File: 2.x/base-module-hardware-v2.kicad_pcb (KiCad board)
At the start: 4 copper layers, 99.7 x 99.7 mm, 276 parts, among them K1 CONN_3, P1 PINBALL-CONNECTOR, P2 PINBALL-CONNECTOR, P3 SOLENOID-CONNECTOR, P4 CONN_16, P5 CONN_16, P6 HE10-34, Q1 BC846, Q10 DMN6040SSD, Q11 BC846, Q12 BC846, Q13 DMP2240UDM, Q14 DMP2240UDM, Q15 BC846, Q16 BC846, Q17 BC846, Q18 BC846, Q19 DMN6040SSD, Q2 BC846, Q20 DMN6040SSD, Q21 BC846, Q22 BC846, Q23 BC846, Q24 BC846, Q25 BC846, Q26 BC846, Q27 BC846, Q28 BC846, Q29 BSS138 DNP, Q3 DMN6040SSD, Q30 FDD5614P, Q31 BC846, Q32 BSS138, Q4 DMN6040SSD, Q5 BC846, Q6 BC846, Q7 BC846, Q8 BC846, Q9 DMN6040SSD, U1 74LVC14, U2 STM32F072R, U3 MCP2562, U4 MC78L05, U5 AP1117IE33G, U6 ZXCT1086E5TA, U7 ZXCT1107SA-7, U8 LM7805CT, U9 MMA8653FC, X1 8.000 MHz

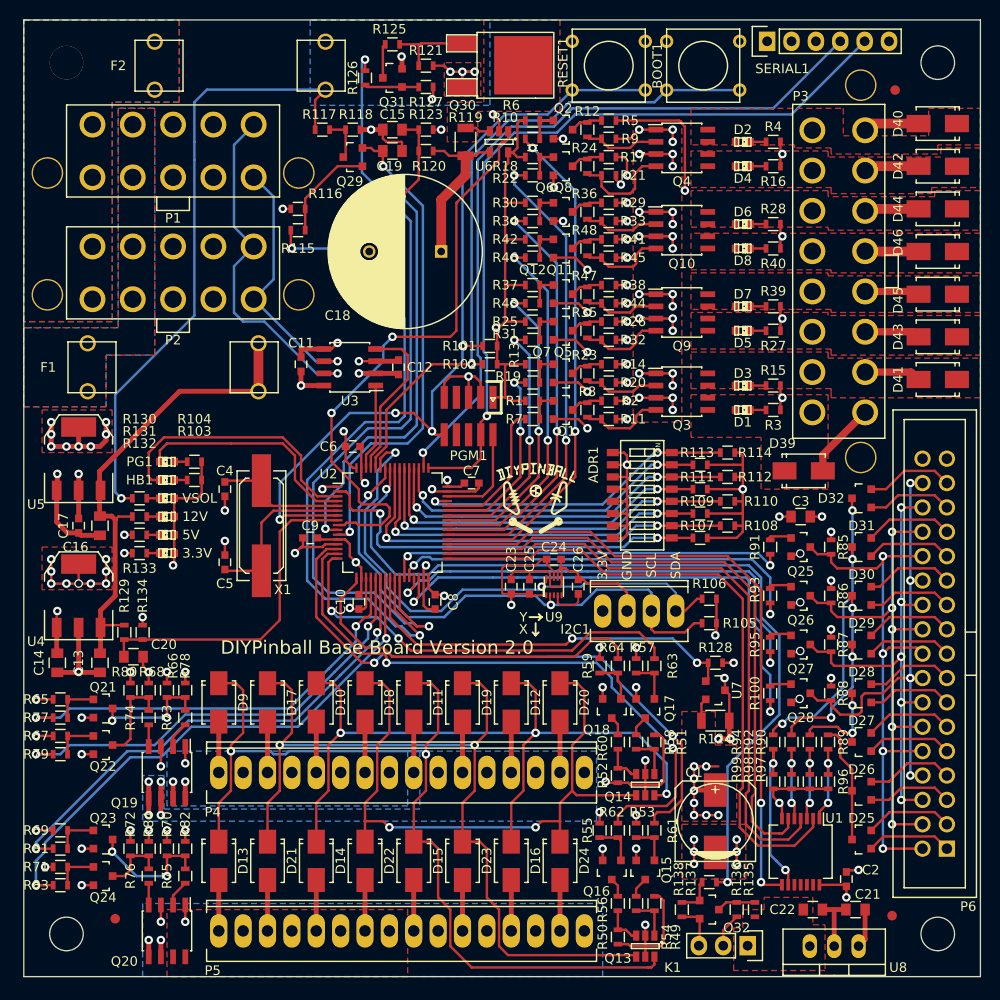
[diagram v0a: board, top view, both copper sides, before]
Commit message: Committing latest files. This includes the KiCAD 4.0.0rc1 migration as well as the updates to Base Board 2.1.
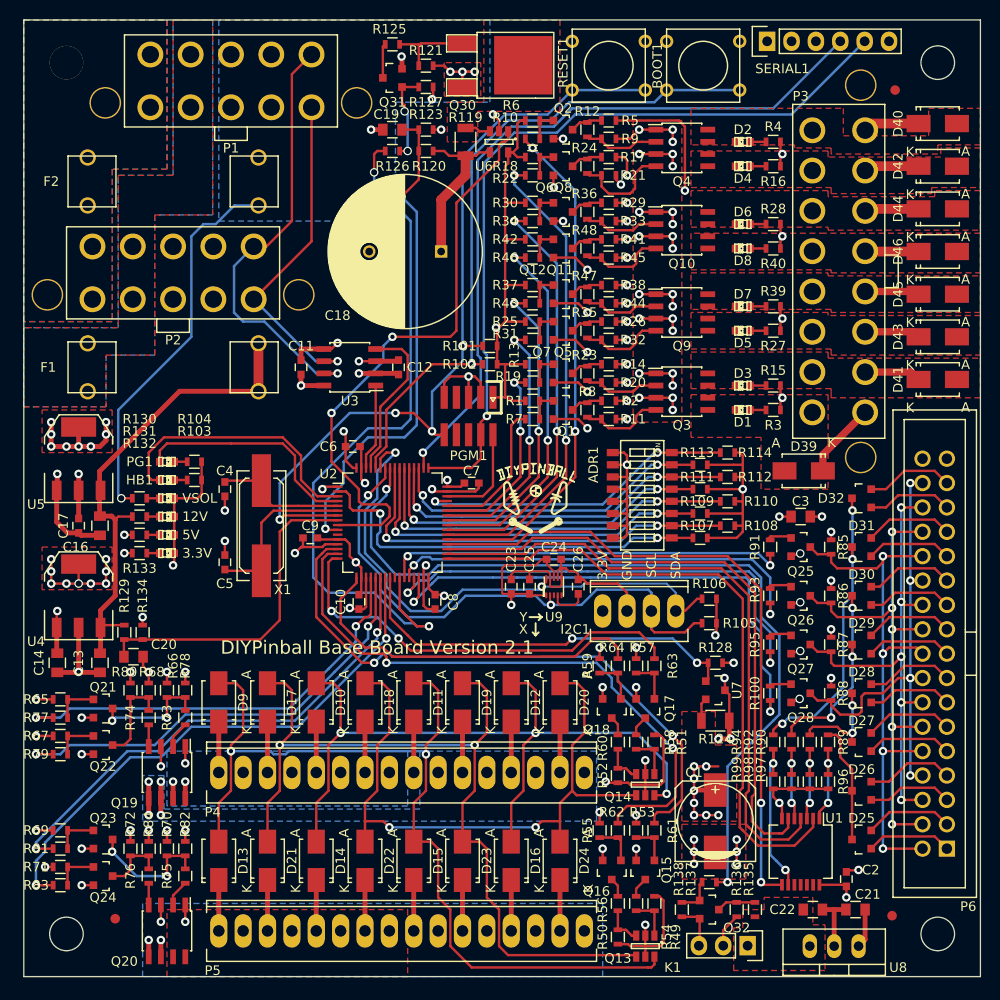
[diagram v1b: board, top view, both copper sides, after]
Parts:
- removed C15: 10u DNP, Capacitors_SMD:C_0805
- removed Q29: BSS138 DNP, Housings_SOT-23_SOT-143_TSOT-6:SOT-23
- removed R115: 1K DNP, Resistors_SMD:R_0603
- removed R116: 10K DNP, Resistors_SMD:R_0603
- removed R117: 95.3K 1% DNP, Resistors_SMD:R_0603
- removed R118: 5.1K 1% DNP, Resistors_SMD:R_0603
- D10, D11, D12, D13, D14, D15, D16, D17, D18, D19, D20, D21, D22, D23, D24, D39, D40, D41, D42, D43, D44, D45, D46, D9: footprint Diodes_SMD:Diode-SMA_Standard -> Diodes_SMD:SMA_Standard
- moved F2 13.9 mm to (71.4, 96.8)
- moved P1 9.47 mm to (77.5, 86.4)
- moved R126 8.14 mm to (94.3, 93.7), turned to 180 degrees
- moved C11 0.32 mm to (84.8, 116.2)
- turned D1 to 0 degrees
- turned D10 to 90 degrees
- turned D11 to 90 degrees
- turned D12 to 90 degrees
- turned D13 to 90 degrees
- turned D14 to 90 degrees
- turned D15 to 90 degrees
- turned D16 to 90 degrees
- turned D17 to 90 degrees
- turned D18 to 90 degrees
- turned D19 to 90 degrees
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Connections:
- net VCC renamed +3.3V
- D12 pad 1: Net-(D10-Pad1) -> Net-(D12-Pad1)
- D12 pad 2: Net-(D12-Pad2) -> Net-(D10-Pad2)
- D13 pad 1: Net-(D11-Pad1) -> Net-(D13-Pad1)
- D13 pad 2: Net-(D13-Pad2) -> Net-(D11-Pad2)
- D14 pad 1: Net-(D10-Pad1) -> Net-(D14-Pad1)
- D14 pad 2: Net-(D14-Pad2) -> Net-(D10-Pad2)
- D15 pad 1: Net-(D11-Pad1) -> Net-(D15-Pad1)
- D15 pad 2: Net-(D15-Pad2) -> Net-(D11-Pad2)
- D16 pad 1: Net-(D10-Pad1) -> Net-(D16-Pad1)
- D16 pad 2: Net-(D16-Pad2) -> Net-(D10-Pad2)
- D19 pad 1: Net-(D17-Pad1) -> Net-(D19-Pad1)
- D19 pad 2: Net-(D19-Pad2) -> Net-(D17-Pad2)
- D20 pad 1: Net-(D18-Pad1) -> Net-(D20-Pad1)
- D20 pad 2: Net-(D20-Pad2) -> Net-(D18-Pad2)
- D21 pad 1: Net-(D17-Pad1) -> Net-(D21-Pad1)
- D21 pad 2: Net-(D21-Pad2) -> Net-(D17-Pad2)
- D22 pad 1: Net-(D18-Pad1) -> Net-(D22-Pad1)
- D22 pad 2: Net-(D22-Pad2) -> Net-(D18-Pad2)
- D23 pad 1: Net-(D17-Pad1) -> Net-(D23-Pad1)
- D23 pad 2: Net-(D23-Pad2) -> Net-(D17-Pad2)
- D24 pad 1: Net-(D18-Pad1) -> Net-(D24-Pad1)
- D24 pad 2: Net-(D24-Pad2) -> Net-(D18-Pad2)
- D35 pad 1: Net-(D35-Pad1) -> GND
- D35 pad 2: GND -> Net-(D35-Pad2)
- D36 pad 1: Net-(D36-Pad1) -> GND
- D36 pad 2: GND -> Net-(D36-Pad2)
- D37 pad 1: Net-(D37-Pad1) -> GND
- D37 pad 2: GND -> Net-(D37-Pad2)
- D38 pad 1: Net-(D38-Pad1) -> GND
- D38 pad 2: GND -> Net-(D38-Pad2)
- D39 pad 1: Net-(D1-Pad2) -> /Solenoid Driver/SOL_PWR
- D39 pad 2: /Solenoid Driver/SOL_PWR -> Net-(D1-Pad1)
- D40 pad 1: Net-(D2-Pad2) -> /Solenoid Driver/SOL_PWR
- D40 pad 2: /Solenoid Driver/SOL_PWR -> Net-(D2-Pad1)
- D41 pad 1: Net-(D3-Pad2) -> /Solenoid Driver/SOL_PWR
- D41 pad 2: /Solenoid Driver/SOL_PWR -> Net-(D3-Pad1)
- D42 pad 1: Net-(D4-Pad2) -> /Solenoid Driver/SOL_PWR
- D42 pad 2: /Solenoid Driver/SOL_PWR -> Net-(D4-Pad1)
- D43 pad 1: Net-(D43-Pad1) -> /Solenoid Driver/SOL_PWR
- D43 pad 2: /Solenoid Driver/SOL_PWR -> Net-(D43-Pad2)
- D44 pad 1: Net-(D44-Pad1) -> /Solenoid Driver/SOL_PWR
- D44 pad 2: /Solenoid Driver/SOL_PWR -> Net-(D44-Pad2)
- D45 pad 1: Net-(D45-Pad1) -> /Solenoid Driver/SOL_PWR
- D45 pad 2: /Solenoid Driver/SOL_PWR -> Net-(D45-Pad2)
- D46 pad 1: Net-(D46-Pad1) -> /Solenoid Driver/SOL_PWR
- D46 pad 2: /Solenoid Driver/SOL_PWR -> Net-(D46-Pad2)
- D5 pad 1: Net-(D5-Pad1) -> Net-(D43-Pad2)
- D5 pad 2: Net-(D43-Pad1) -> Net-(D5-Pad2)
- D6 pad 1: Net-(D6-Pad1) -> Net-(D44-Pad2)
- D6 pad 2: Net-(D44-Pad1) -> Net-(D6-Pad2)
- D7 pad 1: Net-(D7-Pad1) -> Net-(D45-Pad2)
- D7 pad 2: Net-(D45-Pad1) -> Net-(D7-Pad2)
- D8 pad 1: Net-(D8-Pad1) -> Net-(D46-Pad2)
- D8 pad 2: Net-(D46-Pad1) -> Net-(D8-Pad2)
- D9 pad 1: Net-(D11-Pad1) -> Net-(D9-Pad1)
- D9 pad 2: Net-(D9-Pad2) -> Net-(D11-Pad2)
- HB1 pad 1: /Control Logic/HEARTBEAT -> Net-(HB1-Pad1)
- HB1 pad 2: Net-(HB1-Pad2) -> /Control Logic/HEARTBEAT
- P3 pad 1: Net-(D1-Pad2) -> Net-(D1-Pad1)
- P3 pad 2: Net-(D3-Pad2) -> Net-(D3-Pad1)
- P3 pad 3: Net-(D43-Pad1) -> Net-(D43-Pad2)
- P3 pad 4: Net-(D45-Pad1) -> Net-(D45-Pad2)
- P3 pad 5: Net-(D46-Pad1) -> Net-(D46-Pad2)
- P3 pad 6: Net-(D44-Pad1) -> Net-(D44-Pad2)
- P3 pad 7: Net-(D4-Pad2) -> Net-(D4-Pad1)
- P3 pad 8: Net-(D2-Pad2) -> Net-(D2-Pad1)
- P4 pad 1: Net-(D9-Pad2) -> Net-(D9-Pad1)
- P4 pad 11: Net-(D19-Pad2) -> Net-(D19-Pad1)
- P4 pad 13: Net-(D12-Pad2) -> Net-(D12-Pad1)
- P4 pad 15: Net-(D20-Pad2) -> Net-(D20-Pad1)
- P4 pad 3: Net-(D17-Pad2) -> Net-(D17-Pad1)
- P4 pad 5: Net-(D10-Pad2) -> Net-(D10-Pad1)
- P4 pad 7: Net-(D18-Pad2) -> Net-(D18-Pad1)
- P4 pad 9: Net-(D11-Pad2) -> Net-(D11-Pad1)
- P5 pad 1: Net-(D13-Pad2) -> Net-(D13-Pad1)
- P5 pad 11: Net-(D23-Pad2) -> Net-(D23-Pad1)
- P5 pad 13: Net-(D16-Pad2) -> Net-(D16-Pad1)
- P5 pad 15: Net-(D24-Pad2) -> Net-(D24-Pad1)
- P5 pad 3: Net-(D21-Pad2) -> Net-(D21-Pad1)
- P5 pad 5: Net-(D14-Pad2) -> Net-(D14-Pad1)
- P5 pad 7: Net-(D22-Pad2) -> Net-(D22-Pad1)
- P5 pad 9: Net-(D15-Pad2) -> Net-(D15-Pad1)
- P6 pad 33: (no net) -> GND
- P6 pad 34: (no net) -> +12V
- PG1 pad 1: /Control Logic/POWER_GOOD -> Net-(PG1-Pad1)
- PG1 pad 2: Net-(PG1-Pad2) -> /Control Logic/POWER_GOOD
- Q10 pad 5: Net-(D46-Pad1) -> Net-(D46-Pad2)
- Q10 pad 6: Net-(D46-Pad1) -> Net-(D46-Pad2)
- Q10 pad 7: Net-(D44-Pad1) -> Net-(D44-Pad2)
- Q10 pad 8: Net-(D44-Pad1) -> Net-(D44-Pad2)
- Q13 pad 4: Net-(D17-Pad1) -> Net-(D17-Pad2)
- Q13 pad 6: Net-(D11-Pad1) -> Net-(D11-Pad2)
- Q14 pad 4: Net-(D18-Pad1) -> Net-(D18-Pad2)
- Q14 pad 6: Net-(D10-Pad1) -> Net-(D10-Pad2)
- Q3 pad 5: Net-(D1-Pad2) -> Net-(D1-Pad1)
- Q3 pad 6: Net-(D1-Pad2) -> Net-(D1-Pad1)
- Q3 pad 7: Net-(D3-Pad2) -> Net-(D3-Pad1)
- Q3 pad 8: Net-(D3-Pad2) -> Net-(D3-Pad1)
- Q4 pad 5: Net-(D4-Pad2) -> Net-(D4-Pad1)
- Q4 pad 6: Net-(D4-Pad2) -> Net-(D4-Pad1)
- Q4 pad 7: Net-(D2-Pad2) -> Net-(D2-Pad1)
- Q4 pad 8: Net-(D2-Pad2) -> Net-(D2-Pad1)
- Q9 pad 5: Net-(D43-Pad1) -> Net-(D43-Pad2)
- Q9 pad 6: Net-(D43-Pad1) -> Net-(D43-Pad2)
- Q9 pad 7: Net-(D45-Pad1) -> Net-(D45-Pad2)
- Q9 pad 8: Net-(D45-Pad1) -> Net-(D45-Pad2)
- R103 pad 1: Net-(HB1-Pad2) -> Net-(HB1-Pad1)
- R104 pad 1: Net-(PG1-Pad2) -> Net-(PG1-Pad1)
- R130 pad 2: Net-(D35-Pad1) -> Net-(D35-Pad2)
- R131 pad 2: Net-(D36-Pad1) -> Net-(D36-Pad2)
- R132 pad 2: Net-(D37-Pad1) -> Net-(D37-Pad2)
- R133 pad 2: Net-(D38-Pad1) -> Net-(D38-Pad2)
- R15 pad 2: Net-(D3-Pad1) -> Net-(D3-Pad2)
- R16 pad 2: Net-(D4-Pad1) -> Net-(D4-Pad2)
- R27 pad 2: Net-(D5-Pad1) -> Net-(D5-Pad2)
- R28 pad 2: Net-(D6-Pad1) -> Net-(D6-Pad2)
- R3 pad 2: Net-(D1-Pad1) -> Net-(D1-Pad2)
- R39 pad 2: Net-(D7-Pad1) -> Net-(D7-Pad2)
- R4 pad 2: Net-(D2-Pad1) -> Net-(D2-Pad2)
- R40 pad 2: Net-(D8-Pad1) -> Net-(D8-Pad2)
- U2 pad 11: /Control Logic/VSOL_IN_SENSE -> (no net)
- U2 pad 25: /Control Logic/VSOL_MEASURE_CONTROL -> (no net)
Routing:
- net Net-(D11-Pad2): track 5.30 -> 96.7 mm, vias 0 -> 2
- net Net-(D11-Pad1): track 96.7 -> 5.30 mm, vias 2 -> 0
- net Net-(D17-Pad2): track 5.30 -> 87.7 mm, vias 0 -> 2
- net Net-(D17-Pad1): track 87.7 -> 5.30 mm, vias 2 -> 0
- net Net-(D10-Pad2): track 5.30 -> 79.1 mm, vias 0 -> 3
- net Net-(D10-Pad1): track 79.1 -> 5.30 mm, vias 3 -> 0
- net /Control Logic/VSOL_MEASURE_CONTROL: track 71.5 -> 0.00 mm, vias 2 -> 0
- net Net-(D18-Pad1): track 67.1 -> 5.30 mm, vias 2 -> 0
- net Net-(D18-Pad2): track 5.30 -> 67.1 mm, vias 0 -> 2
- net /Control Logic/VSOL_IN_SENSE: track 50.5 -> 0.00 mm, vias 2 -> 0
- net (no net): track 29.3 -> 0.11 mm
- net VEE: track 72.4 -> 47.6 mm
- net Net-(Q29-Pad1): track 10.7 -> 0.00 mm
- net /Control Logic/VSOL_PRECHARGE_PWM: track 84.9 -> 74.5 mm
- net /Control Logic/CANH: track 37.0 -> 45.9 mm
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- added copper zone on F.Cu, net Net-(D1-Pad1)
- added copper zone on F.Cu, net Net-(D2-Pad1)
- added copper zone on F.Cu, net Net-(D3-Pad1)
- added copper zone on F.Cu, net Net-(D4-Pad1)
- added copper zone on F.Cu, net Net-(D43-Pad2)
- added copper zone on F.Cu, net Net-(D44-Pad2)
- added copper zone on F.Cu, net Net-(D45-Pad2)
- added copper zone on F.Cu, net Net-(D46-Pad2)
- added copper zone on F.Cu, net VCC
- removed copper zone on F.Cu, net +3.3V
- removed copper zone on F.Cu, net Net-(D1-Pad2)
- removed copper zone on F.Cu, net Net-(D2-Pad2)
- removed copper zone on F.Cu, net Net-(D3-Pad2)
- removed copper zone on F.Cu, net Net-(D4-Pad2)
- removed copper zone on F.Cu, net Net-(D43-Pad1)
- removed copper zone on F.Cu, net Net-(D44-Pad1)
- removed copper zone on F.Cu, net Net-(D45-Pad1)
- removed copper zone on F.Cu, net Net-(D46-Pad1)
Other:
- board text added: "DIYPinball Base Board Version 2.1"
- board text removed: "CANH"
- board text removed: "CANL"
- board text removed: "DIYPinball Base Board Version 2.0"
